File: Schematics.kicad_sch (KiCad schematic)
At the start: 73 parts, among them Q1 AO3400A, Q2 SI2301CDS-T1-E3, Q3 SI2301CDS-T1-E3, Q4 8050, U2 CAT24C32, U3 ME6217C33M5G, U6 TXB0108PWR

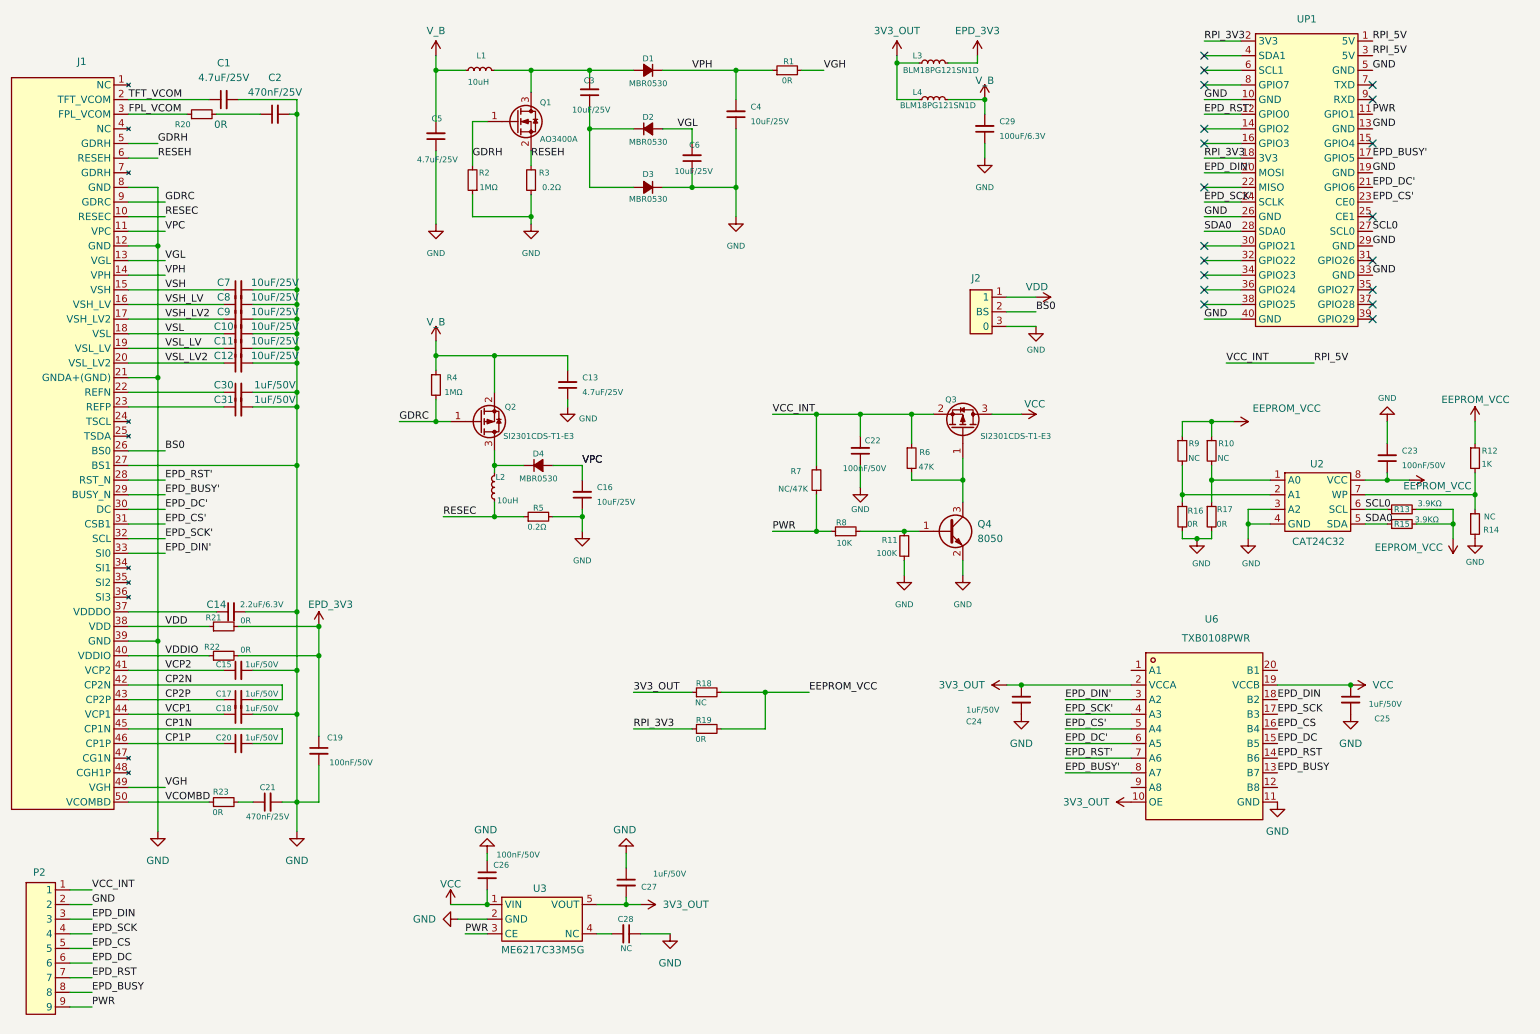
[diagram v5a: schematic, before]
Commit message: made changes to simplify the board
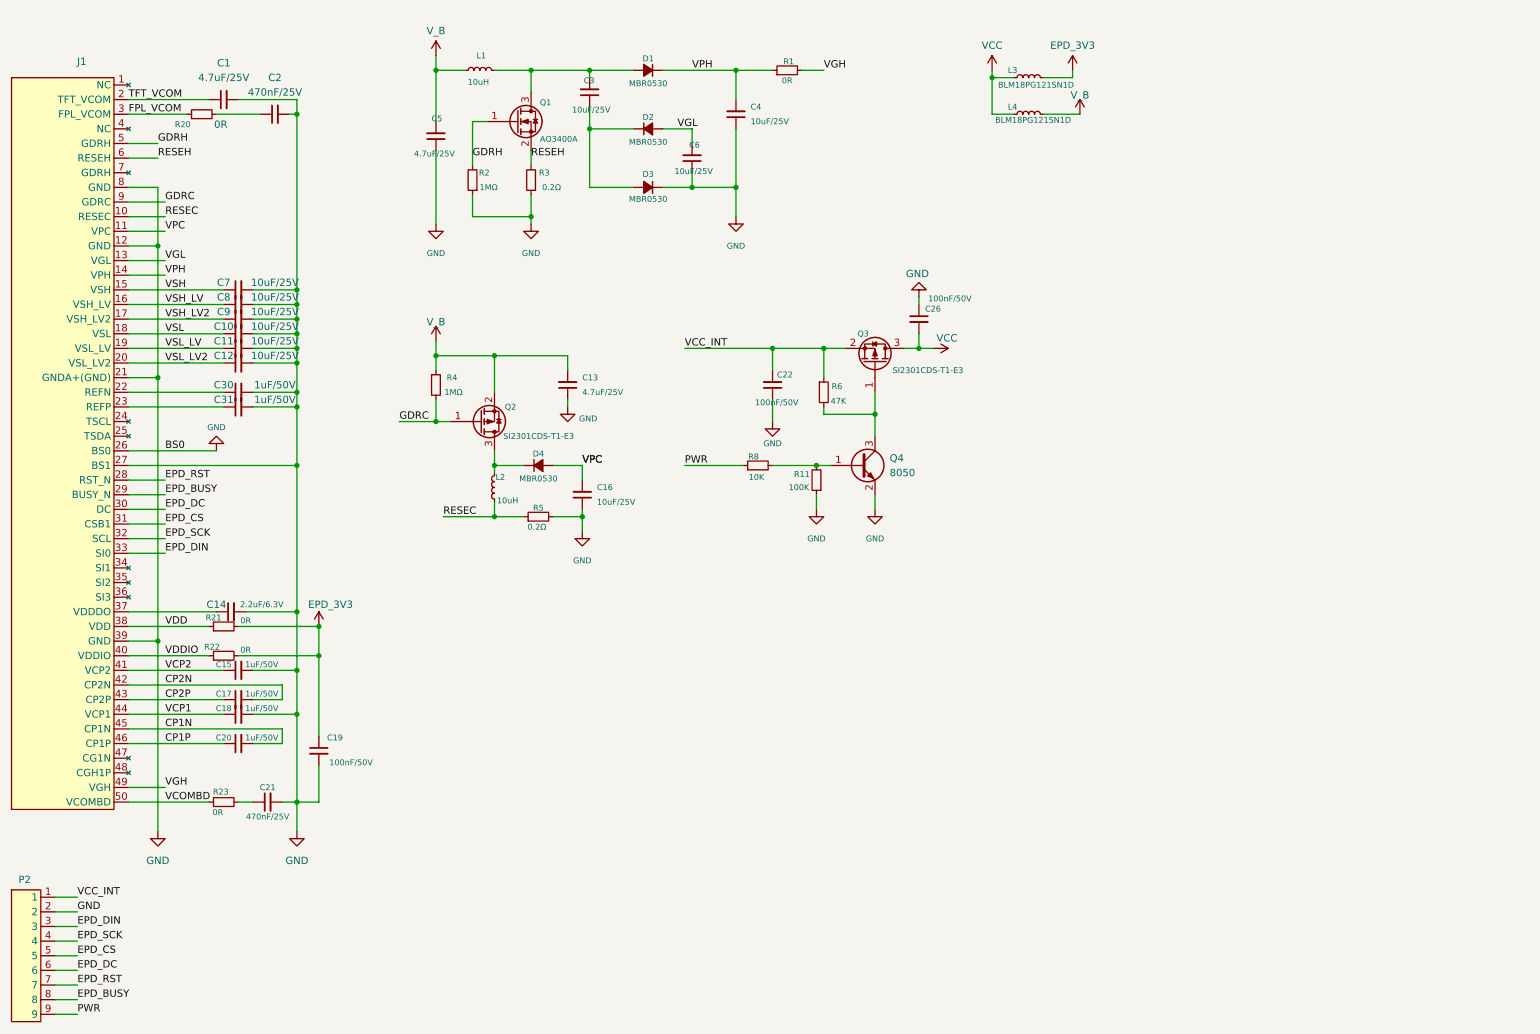
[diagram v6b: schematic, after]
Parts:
- removed C23: 100nF/50V, Capacitor_SMD:C_0603_1608Metric, symbol Device:C_Small
- removed C24, C25, C27: 1uF/50V, Capacitor_SMD:C_0603_1608Metric, symbol Device:C_Small
- removed C28: NC, Capacitor_SMD:C_0603_1608Metric, symbol Device:C_Small
- removed C29: 100uF/6.3V, Capacitor_SMD:C_1206_3216Metric, symbol Device:C_Small
- removed J2: (no value), Connector_PinSocket_2.54mm:PinSocket_1x03_P2.54mm_Vertical, symbol Hat_Eink_Esp32:Eink_Esp32_Switch
- removed R10, R14, R18, R9: NC, Resistor_SMD:R_0603_1608Metric, symbol Device:R_Small
- removed R12: 1K, Resistor_SMD:R_0603_1608Metric, symbol Device:R_Small
- removed R13, R15: 3.9KΩ, Resistor_SMD:R_0603_1608Metric, symbol Device:R_Small
- removed R16, R17, R19: 0R, Resistor_SMD:R_0603_1608Metric, symbol Device:R_Small
- removed R7: NC/47K, Resistor_SMD:R_0603_1608Metric, symbol Device:R_Small
- removed U2: CAT24C32, local:SOIC-8_L5.0-W4.0-P1.27-LS6.0-BL, symbol Hat_Eink_Esp32:Eink_Esp32_CAT24C32
- removed U3: ME6217C33M5G, local:SOT-23-5_L3.0-W1.7-P0.95-LS2.8-BR, symbol Hat_Eink_Esp32:Eink_Esp32_ME6217C33M5G
- removed U6: TXB0108PWR, local:TSSOP-20_L6.5-W4.4-P0.65-LS6.4-BL, symbol local:TXB0108PWR
- removed UP1: (no value), local:HDR-SMD_40P-P2.54-V-F-R2-C20-S2.54-LS7.1, symbol Hat_Eink_Esp32:Eink_Esp32_Rpi
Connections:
- net 3V3_OUT is gone; now on net VCC: L3.1, L4.1
- net BS0 is gone; now on net GND: J1.26 (BS0)
- net EPD_BUSY' is gone; now on net EPD_BUSY: J1.29 (BUSY_N)
- net EPD_CS' is gone; now on net EPD_CS: J1.31 (CSB1)
- net EPD_DC' is gone; now on net EPD_DC: J1.30 (DC)
- net EPD_DIN' is gone; now on net EPD_DIN: J1.33 (SI0)
- net EPD_RST' is gone; now on net EPD_RST: J1.28 (RST_N)
- net EPD_SCK' is gone; now on net EPD_SCK: J1.32 (SCL)
- net RPI_5V renamed VCC_INT
- no-connect marks 19 -> 0
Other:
- moved on the sheet: C22, C26, L3, L4, P2, Q3, Q4, R11, R6, R8

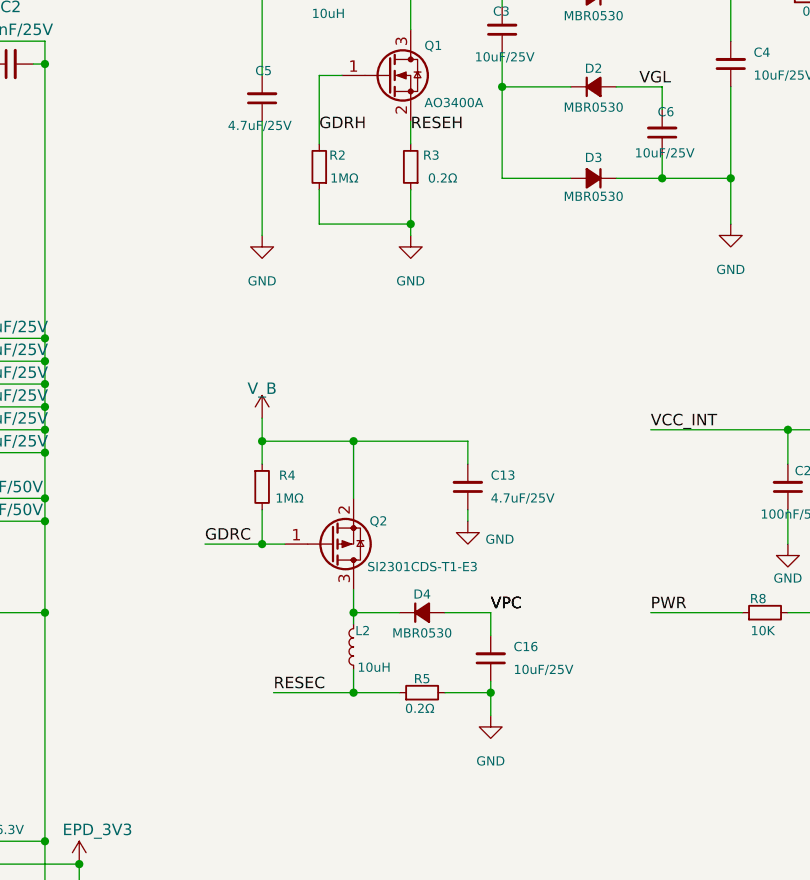
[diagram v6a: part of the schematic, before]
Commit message: completed minimalist schematics and PCB of epaper
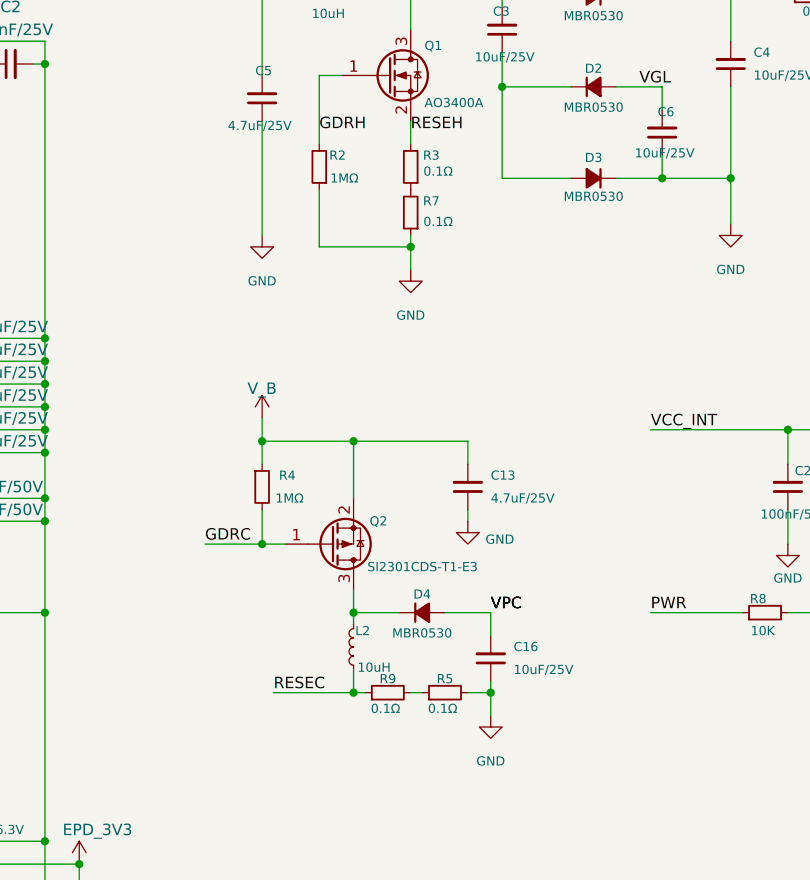
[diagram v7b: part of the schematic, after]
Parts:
- added R7, R9: 0.1Ω, Resistor_SMD:R_0603_1608Metric, symbol Device:R_Small
- C1, C13, C5: footprint Capacitor_SMD:C_0603_1608Metric -> Capacitor_SMD:C_0805_2012Metric
- C14: footprint Capacitor_SMD:C_0603_1608Metric -> Capacitor_SMD:C_0402_1005Metric
- D1, D2, D3, D4: footprint local:SOD-123_L2.8-W1.8-LS3.7-RD -> local:SOD-123_L2.7-W1.6-LS3.7-RD-1
- L1, L2: footprint Inductor_SMD:L_1008_2520Metric -> local:L0805
- R3, R5: value 0.2Ω -> 0.1Ω
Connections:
- net GND: now also R7.1; no longer R3.1
- net RESEC: now also R9.1; no longer R5.1
- new net: R5.1, R9.2
- new net: R3.1, R7.2
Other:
- moved on the sheet: R5
